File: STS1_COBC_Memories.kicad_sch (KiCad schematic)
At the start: 7 parts, among them J5 Flash_Dbg, U1 W25Q01JVZEIQ, U17 CY15B108QN-40SXI

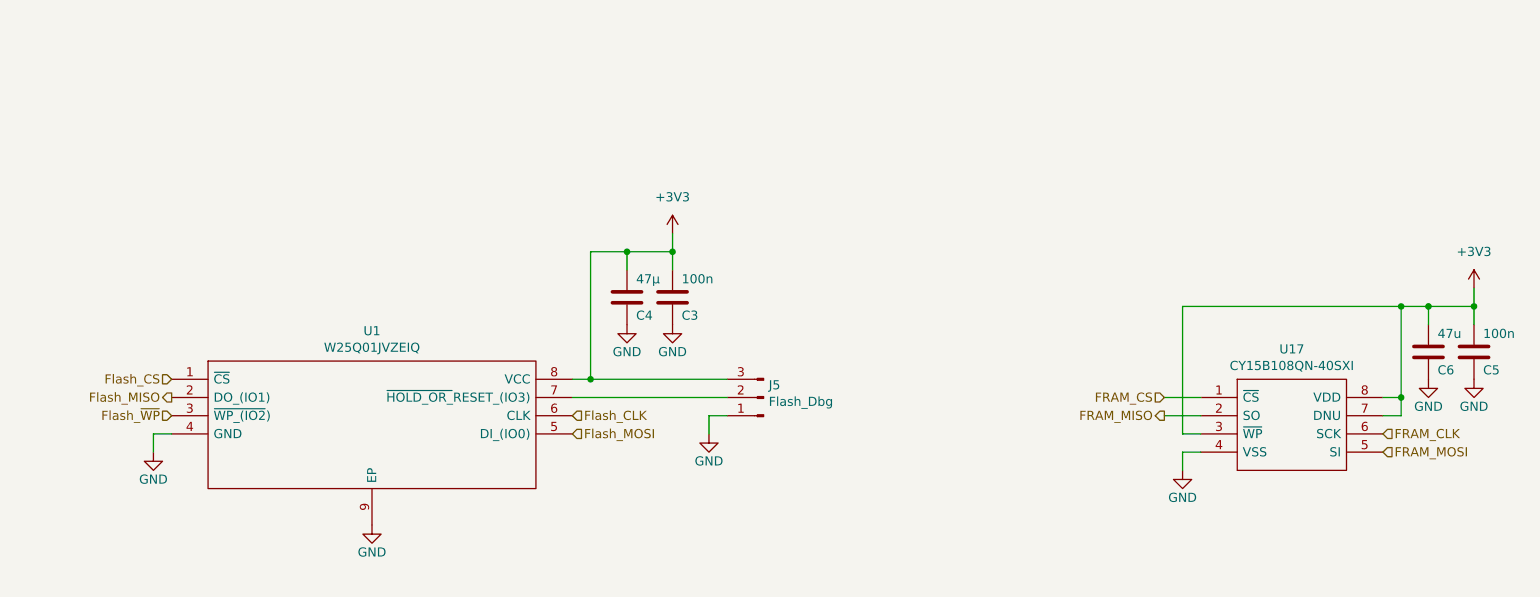
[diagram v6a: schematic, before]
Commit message: Reorganize and clean-up the components around the STM. Pinout changes: 1) Flash_CS moved from PB9 to PA4 2) Dosi_En added on PB10 3) EDU_Boot_Pin added on PB2 4) WDT_Clear moved from PA9 to PB9
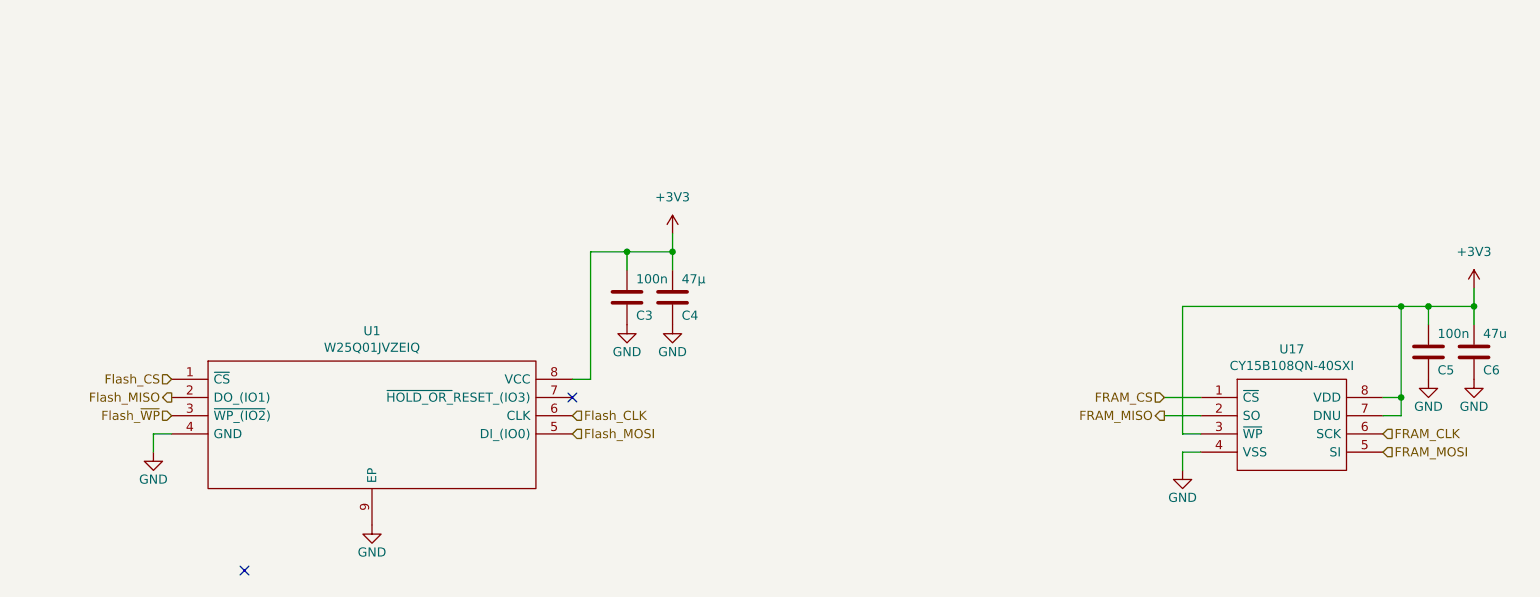
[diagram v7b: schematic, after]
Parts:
- removed J5: Flash_Dbg, STS1library:PinHeader_1x03_P2.54mm_Vertical_umdieEcke, symbol Connector:Conn_01x03_Male
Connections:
- no-connect marks 0 -> 2
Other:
- moved on the sheet: C3, C4, C5, C6
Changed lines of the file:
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@@
 (kicad_sch (version 20211123) (generator eeschema)
   (paper "A4")
-  (junction (at 111.76 71.12) (diameter 0) (color 0 0 0 0)
-  )
   (junction (at 116.84 53.34) (diameter 0) (color 0 0 0 0)
   )
@@
   (junction (at 224.79 60.96) (diameter 0) (color 0 0 0 0)
   )
+  (no_connect (at 63.5 97.79))
+  (no_connect (at 109.22 73.66))
   (wire (pts (xy 222.25 76.2) (xy 224.79 76.2))
     (stroke (width 0) (type default) (color 0 0 0 0))
@@
     (stroke (width 0) (type default) (color 0 0 0 0))
   )
-  (wire (pts (xy 109.22 73.66) (xy 130.81 73.66))
-    (stroke (width 0) (type default) (color 0 0 0 0))
-  )
   (wire (pts (xy 50.8 81.28) (xy 50.8 78.74))
     (stroke (width 0) (type default) (color 0 0 0 0))
@@
     (stroke (width 0) (type default) (color 0 0 0 0))
   )
-  (wire (pts (xy 111.76 71.12) (xy 130.81 71.12))
-    (stroke (width 0) (type default) (color 0 0 0 0))
-  )
-  (wire (pts (xy 128.27 76.2) (xy 130.81 76.2))
-    (stroke (width 0) (type default) (color 0 0 0 0))
-  )
   (wire (pts (xy 194.31 81.28) (xy 196.85 81.28))
     (stroke (width 0) (type default) (color 0 0 0 0))
@@
   )
   (wire (pts (xy 224.79 60.96) (xy 224.79 73.66))
-    (stroke (width 0) (type default) (color 0 0 0 0))
-  )
-  (wire (pts (xy 128.27 78.74) (xy 128.27 76.2))
     (stroke (width 0) (type default) (color 0 0 0 0))
   )
@@
     (pin "8")
   )
+  (symbol (lib_id "Device:C") (at 116.84 59.69 180) (unit 1)
+    (in_bom yes) (on_board yes)
+    (property "Reference" "C3" (id 0) (at 118.11 62.23 0)
+      (effects (font (size 1.27 1.27)) (justify right))
+    )
+    (property "Value" "100n" (id 1) (at 118.11 57.15 0)
+      (effects (font (size 1.27 1.27)) (justify right))
+    )
+    (property "Footprint" "Capacitor_SMD:C_0603_1608Metric" (id 2) (at 115.8748 55.88 0)
+      (effects (font (size 1.27 1.27)) hide)
+    )
+    (property "Datasheet" "~" (id 3) (at 116.84 59.69 0)
+      (effects (font (size 1.27 1.27)) hide)
+    )
+    (pin "1")
+    (pin "2")
+  )
   (symbol (lib_id "Device:C") (at 123.19 59.69 180) (unit 1)
     (in_bom yes) (on_board yes)
-    (property "Reference" "C3" (id 0) (at 124.46 62.23 0)
-      (effects (font (size 1.27 1.27)) (justify right))
-    )
-    (property "Value" "100n" (id 1) (at 124.46 57.15 0)
+    (property "Reference" "C4" (id 0) (at 124.46 62.23 0)
+      (effects (font (size 1.27 1.27)) (justify right))
+    )
+    (property "Value" "47µ" (id 1) (at 124.46 57.15 0)
       (effects (font (size 1.27 1.27)) (justify right))
     )
@@
     (pin "2")
   )
-  (symbol (lib_id "Device:C") (at 116.84 59.69 180) (unit 1)
-    (in_bom yes) (on_board yes)
-    (property "Reference" "C4" (id 0) (at 118.11 62.23 0)
-      (effects (font (size 1.27 1.27)) (justify right))
-    )
-    (property "Value" "47µ" (id 1) (at 118.11 57.15 0)
-      (effects (font (size 1.27 1.27)) (justify right))
-    )
-    (property "Footprint" "Capacitor_SMD:C_0603_1608Metric" (id 2) (at 115.8748 55.88 0)
-      (effects (font (size 1.27 1.27)) hide)
-    )
-    (property "Datasheet" "~" (id 3) (at 116.84 59.69 0)
+  (symbol (lib_id "Device:C") (at 228.6 67.31 180) (unit 1)
+    (in_bom yes) (on_board yes)
+    (property "Reference" "C5" (id 0) (at 229.87 69.85 0)
+      (effects (font (size 1.27 1.27)) (justify right))
+    )
+    (property "Value" "100n" (id 1) (at 229.87 64.77 0)
+      (effects (font (size 1.27 1.27)) (justify right))
+    )
+    (property "Footprint" "Capacitor_SMD:C_0603_1608Metric" (id 2) (at 227.6348 63.5 0)
+      (effects (font (size 1.27 1.27)) hide)
+    )
+    (property "Datasheet" "~" (id 3) (at 228.6 67.31 0)
       (effects (font (size 1.27 1.27)) hide)
     )
@@
   (symbol (lib_id "Device:C") (at 234.95 67.31 180) (unit 1)
     (in_bom yes) (on_board yes)
-    (property "Reference" "C5" (id 0) (at 236.22 69.85 0)
-      (effects (font (size 1.27 1.27)) (justify right))
-    )
-    (property "Value" "100n" (id 1) (at 236.22 64.77 0)
+    (property "Reference" "C6" (id 0) (at 236.22 69.85 0)
+      (effects (font (size 1.27 1.27)) (justify right))
+    )
+    (property "Value" "47u" (id 1) (at 236.22 64.77 0)
       (effects (font (size 1.27 1.27)) (justify right))
     )
@@
     (pin "2")
   )
-  (symbol (lib_id "Device:C") (at 228.6 67.31 180) (unit 1)
-    (in_bom yes) (on_board yes)
-    (property "Reference" "C6" (id 0) (at 229.87 69.85 0)
-      (effects (font (size 1.27 1.27)) (justify right))
-    )
-    (property "Value" "47u" (id 1) (at 229.87 64.77 0)
-      (effects (font (size 1.27 1.27)) (justify right))
-    )
-    (property "Footprint" "Capacitor_SMD:C_0603_1608Metric" (id 2) (at 227.6348 63.5 0)
-      (effects (font (size 1.27 1.27)) hide)
-    )
-    (property "Datasheet" "~" (id 3) (at 228.6 67.31 0)
-      (effects (font (size 1.27 1.27)) hide)
-    )
-    (pin "1")
-    (pin "2")
-  )
-  (symbol (lib_id "power:GND") (at 128.27 78.74 0) (unit 1)
-    (in_bom yes) (on_board yes)
-    (property "Reference" "#PWR020" (id 0) (at 128.27 85.09 0)
-      (effects (font (size 1.27 1.27)) hide)
-    )
-    (property "Value" "GND" (id 1) (at 128.27 82.55 0))
-    (property "Footprint" "" (id 2) (at 128.27 78.74 0)
-      (effects (font (size 1.27 1.27)) hide)
-    )
-    (property "Datasheet" "" (id 3) (at 128.27 78.74 0)
-      (effects (font (size 1.27 1.27)) hide)
-    )
-    (pin "1")
-  )
-  (symbol (lib_id "Connector:Conn_01x03_Male") (at 135.89 73.66 180) (unit 1)
-    (in_bom yes) (on_board yes)
-    (property "Reference" "J5" (id 0) (at 136.6012 71.9328 0)
-      (effects (font (size 1.27 1.27)) (justify right))
-    )
-    (property "Value" "Flash_Dbg" (id 1) (at 136.6012 74.2442 0)
-      (effects (font (size 1.27 1.27)) (justify right))
-    )
-    (property "Footprint" "STS1library:PinHeader_1x03_P2.54mm_Vertical_umdieEcke" (id 2) (at 135.89 73.66 0)
-      (effects (font (size 1.27 1.27)) hide)
-    )
-    (property "Datasheet" "~" (id 3) (at 135.89 73.66 0)
-      (effects (font (size 1.27 1.27)) hide)
-    )
-    (pin "1")
-    (pin "2")
-    (pin "3")
-  )
   (symbol (lib_id "power:+3V3") (at 123.19 50.8 0) (unit 1)

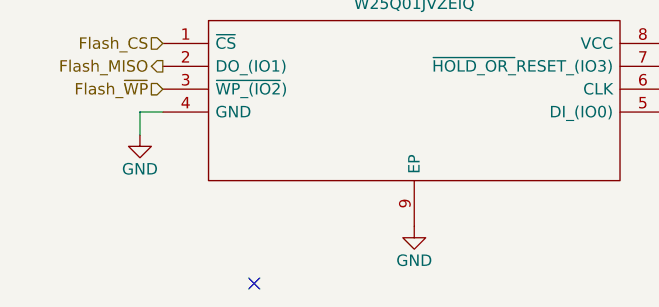
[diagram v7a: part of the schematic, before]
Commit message: Add latchup protection circuits
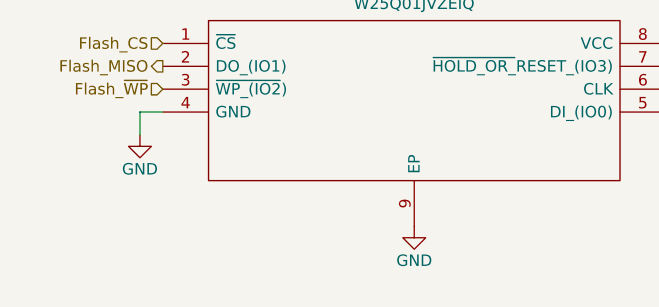
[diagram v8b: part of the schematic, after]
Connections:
- no-connect marks 2 -> 1
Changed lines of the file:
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@@
   (junction (at 224.79 60.96) (diameter 0) (color 0 0 0 0)
   )
-  (no_connect (at 63.5 97.79))
   (no_connect (at 109.22 73.66))
   (wire (pts (xy 222.25 76.2) (xy 224.79 76.2))
